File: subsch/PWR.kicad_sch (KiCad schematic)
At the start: 4 parts, among them U3 HX9193

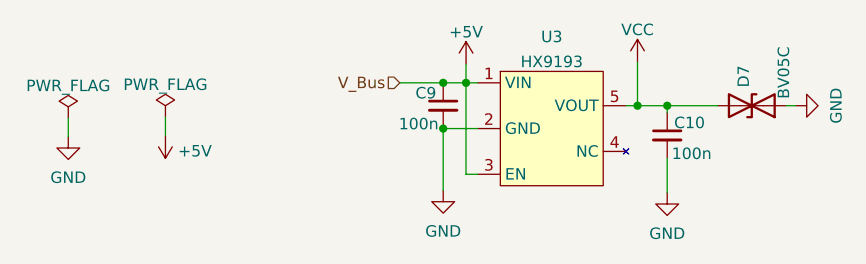
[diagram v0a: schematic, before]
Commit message: Change connectors back to GH1.25&Add ESD for UART and CAN
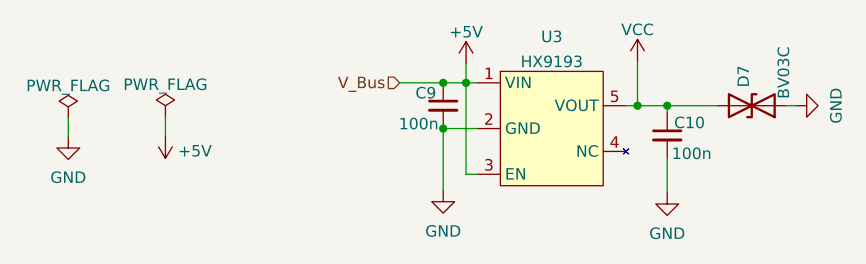
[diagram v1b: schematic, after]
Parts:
- D7: value BV05C -> BV03C
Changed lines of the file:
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@@
       (effects (font (size 1.27 1.27)) (justify right))
     )
-    (property "Value" "BV05C" (at 172.466 76.708 90)
+    (property "Value" "BV03C" (at 172.466 76.708 90)
       (effects (font (size 1.27 1.27)) (justify right))
     )
